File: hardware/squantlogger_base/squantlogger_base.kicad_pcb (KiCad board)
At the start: 2 copper layers, 2 parts, among them M1 FUTURLEC_PB1PB1, U1 USB-micro

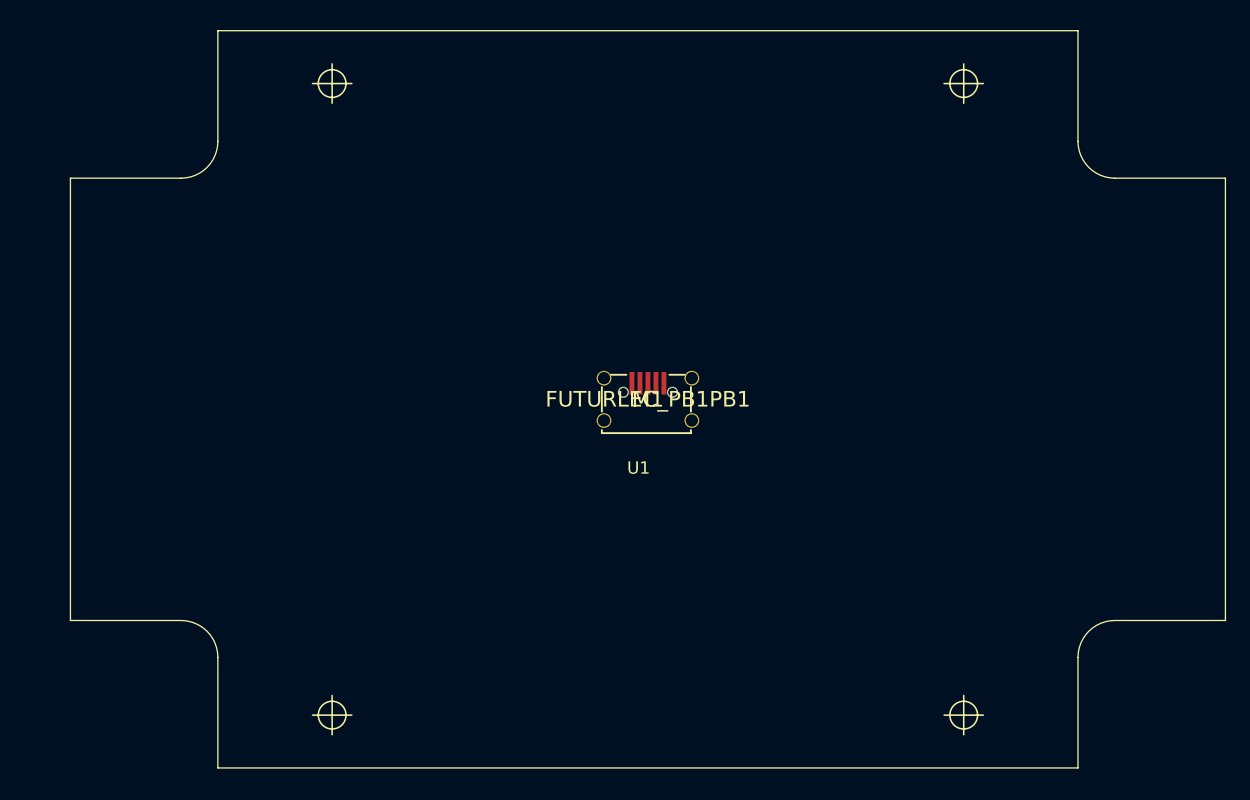
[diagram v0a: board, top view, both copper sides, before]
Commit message: * started with mechanical bits of the squantlogger base, connectors and bits
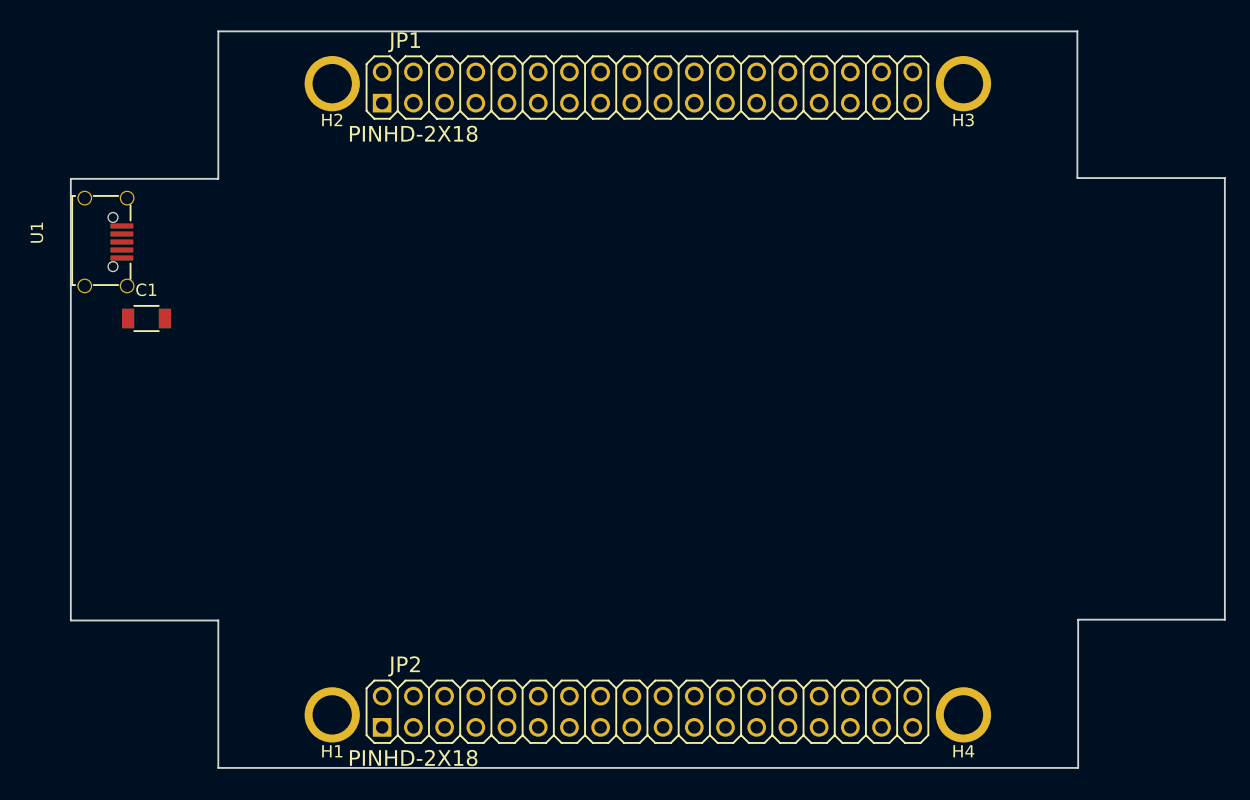
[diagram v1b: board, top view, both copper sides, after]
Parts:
- removed M1: FUTURLEC_PB1PB1, SquantorPcbOutline:SquantorPCBOutline-FUTURLEC_PB1
- added C1: 100n, Capacitors_SMD:C_1206, F.Cu at (107.7, 98.4)
- added H1: Drill_Hole, SquantorPcbOutline:Drill_Hole_PB1, F.Cu at (122.8, 130.7)
- added H2: Drill_Hole, SquantorPcbOutline:Drill_Hole_PB1, F.Cu at (122.8, 79.3)
- added H3: Drill_Hole, SquantorPcbOutline:Drill_Hole_PB1, F.Cu at (174.2, 79.3)
- added H4: Drill_Hole, SquantorPcbOutline:Drill_Hole_PB1, F.Cu at (174.2, 130.7)
- added JP1: PINHD-2X18, SquantorConnectors:SquantorConnectors-2X18, F.Cu at (148.5, 79.6)
- added JP2: PINHD-2X18, SquantorConnectors:SquantorConnectors-2X18, F.Cu at (148.5, 130.4)
- moved U1 45.9 mm to (104.4, 92.2), turned to 270 degrees
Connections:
- U1 pad 5: (no net) -> GND
- U1 pad S: (no net) -> Earth
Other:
- board outline added: 93.9 x 59.9 mm
